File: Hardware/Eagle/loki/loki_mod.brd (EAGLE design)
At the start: 21.9 x 22.9 mm, 39 parts

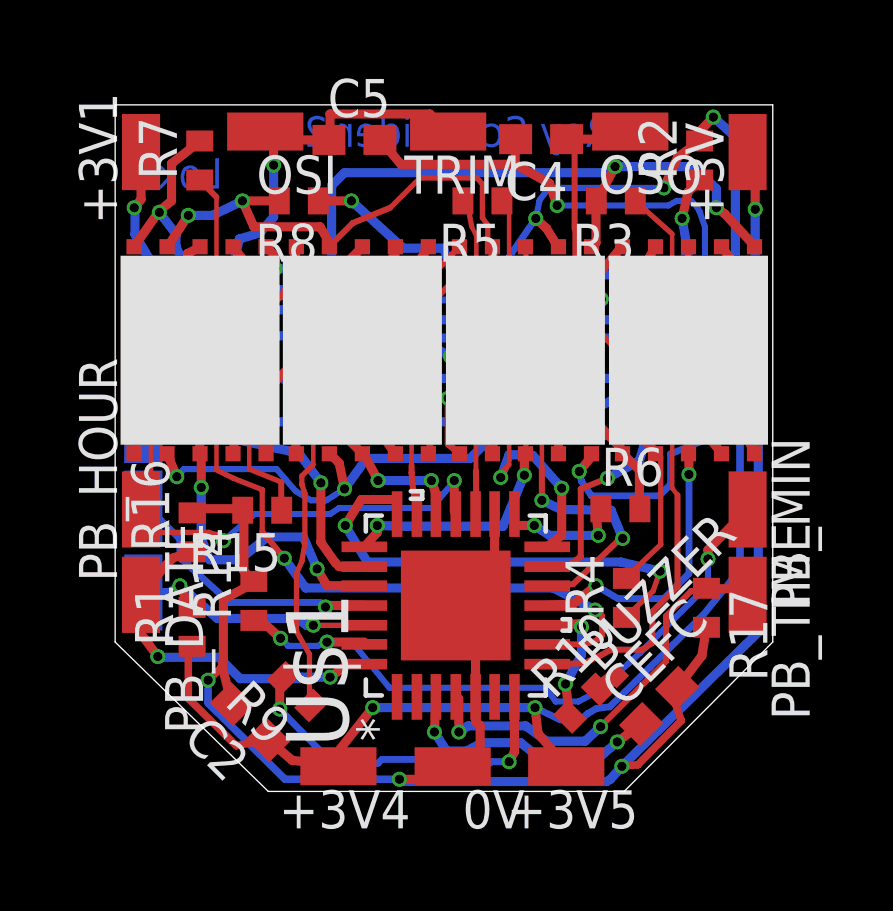
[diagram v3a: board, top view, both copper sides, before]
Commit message: Eliminated one display pin pass-through.
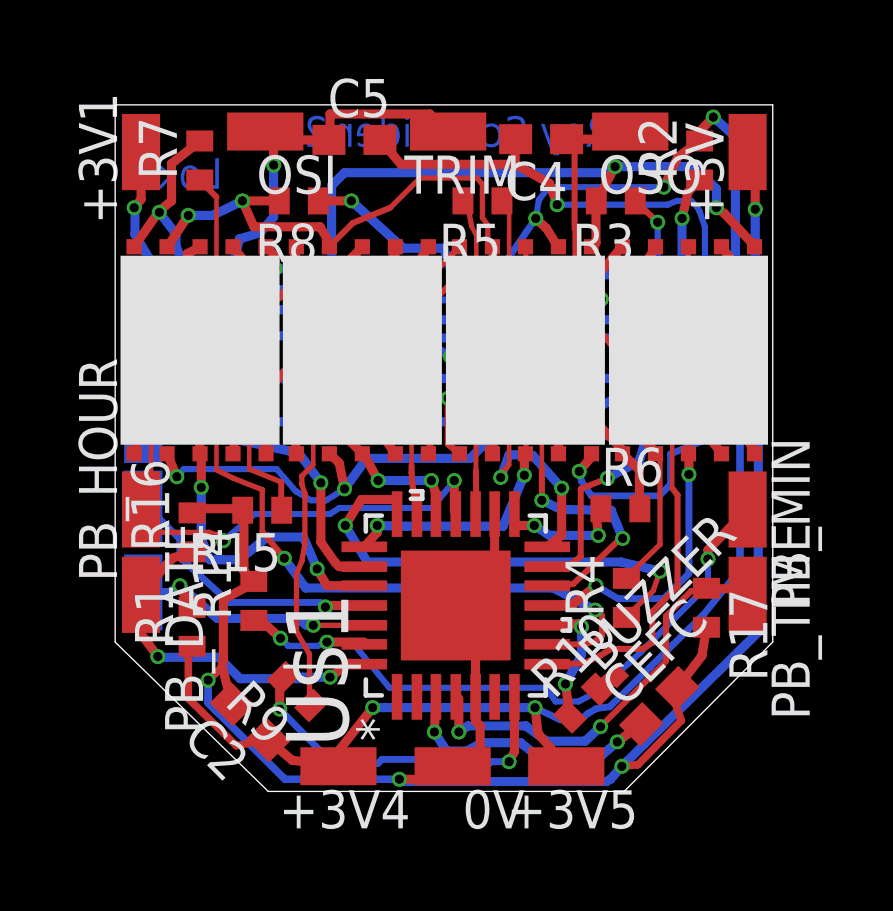
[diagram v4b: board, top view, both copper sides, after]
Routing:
- net RC4/LED_M3: track 20.8 -> 21.5 mm
- net RC5/LED_M2: track 15.2 -> 14.8 mm, vias 2 -> 4
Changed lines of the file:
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@@
 <wire x1="11.176" y1="0.635" x2="11.2268" y2="0.6858" width="0.1524" layer="1"/>
 <wire x1="14.4526" y1="20.1168" x2="13.3096" y2="20.7518" width="0.3048" layer="1"/>
-<wire x1="14.7066" y1="19.3802" x2="14.4526" y2="20.1168" width="0.3048" layer="1"/>
+<wire x1="14.7066" y1="19.4056" x2="14.4526" y2="20.1168" width="0.3048" layer="1"/>
 <wire x1="19.6342" y1="15.6464" x2="19.6342" y2="18.669" width="0.2032" layer="16"/>
 <wire x1="21.4122" y1="14.1986" x2="19.6342" y2="15.6464" width="0.3048" layer="1"/>
@@
 <via x="16.8656" y="0.6858" extent="1-16" drill="0.3048"/>
 <via x="9.4488" y="0.254" extent="1-16" drill="0.3048"/>
-<via x="14.7066" y="19.3802" extent="1-16" drill="0.3048"/>
+<via x="14.7066" y="19.4056" extent="1-16" drill="0.3048"/>
 <via x="19.6342" y="15.6464" extent="1-16" drill="0.3048"/>
 <via x="21.4122" y="12.6238" extent="1-16" drill="0.3048"/>
@@
 <wire x1="19.3802" y1="19.3294" x2="19.177" y2="19.5326" width="0.2032" layer="16"/>
 <wire x1="19.177" y1="19.5326" x2="18.6944" y2="19.5326" width="0.2032" layer="16"/>
-<wire x1="18.6944" y1="19.5326" x2="18.415" y2="19.3802" width="0.2032" layer="16"/>
-<wire x1="18.415" y1="19.3802" x2="14.7066" y2="19.3802" width="0.2032" layer="16"/>
+<wire x1="18.6944" y1="19.5326" x2="18.3896" y2="19.4056" width="0.2032" layer="16"/>
+<wire x1="18.3896" y1="19.4056" x2="14.7066" y2="19.4056" width="0.2032" layer="16"/>
 <wire x1="11.9888" y1="2.9972" x2="11.9888" y2="2.1844" width="0.3048" layer="1"/>
 <wire x1="11.9888" y1="2.1844" x2="12.1412" y2="2.032" width="0.3048" layer="1"/>
@@
 <wire x1="19.0754" y1="19.8374" x2="19.4564" y2="20.2184" width="0.3048" layer="1"/>
 <wire x1="18.8722" y1="18.9484" x2="19.0754" y2="19.8374" width="0.3048" layer="1"/>
-<wire x1="19.0754" y1="17.78" x2="18.8722" y2="18.9484" width="0.3048" layer="16"/>
-<wire x1="17.2974" y1="15.5702" x2="19.0754" y2="17.78" width="0.3048" layer="16"/>
-<wire x1="14.9606" y1="15.5702" x2="17.2974" y2="15.5702" width="0.3048" layer="16"/>
+<wire x1="18.8722" y1="16.891" x2="18.8722" y2="18.9484" width="0.3048" layer="16"/>
+<wire x1="18.6182" y1="15.5702" x2="18.8722" y2="16.891" width="0.3048" layer="16"/>
+<wire x1="14.9606" y1="15.5702" x2="18.6182" y2="15.5702" width="0.3048" layer="16"/>
 <wire x1="14.0716" y1="14.732" x2="14.9606" y2="15.5702" width="0.1778" layer="1"/>
 <wire x1="14.0716" y1="11.684" x2="14.0716" y2="14.732" width="0.1778" layer="1"/>
@@
 <contactref element="U$1" pad="13"/>
 <contactref element="R3" pad="1"/>
-<wire x1="17.907" y1="14.5796" x2="18.542" y2="15.4432" width="0.2032" layer="1"/>
-<wire x1="17.907" y1="12.4206" x2="17.907" y2="14.5796" width="0.2032" layer="1"/>
+<wire x1="17.907" y1="12.4206" x2="17.907" y2="16.256" width="0.2032" layer="1"/>
 <wire x1="17.4498" y1="10.8712" x2="17.907" y2="12.4206" width="0.3048" layer="16"/>
 <wire x1="16.383" y1="10.287" x2="17.4498" y2="10.8712" width="0.3048" layer="16"/>
@@
 <via x="17.907" y="12.4206" extent="1-16" drill="0.3048"/>
 <via x="16.383" y="10.287" extent="1-16" drill="0.3048"/>
-<wire x1="18.542" y1="15.4432" x2="18.542" y2="18.43" width="0.1524" layer="1"/>
-<wire x1="18.542" y1="18.43" x2="17.3124" y2="19.5326" width="0.1778" layer="1"/>
+<via x="17.907" y="16.256" extent="1-16" drill="0.3048"/>
+<wire x1="17.907" y1="16.256" x2="18.1356" y2="17.018" width="0.2032" layer="16"/>
+<wire x1="18.1356" y1="17.018" x2="18.0594" y2="17.7038" width="0.2032" layer="16"/>
+<wire x1="18.0594" y1="17.7038" x2="18.0594" y2="18.8214" width="0.2032" layer="16"/>
+<via x="18.0594" y="18.8214" extent="1-16" drill="0.3048"/>
+<wire x1="18.0594" y1="18.8214" x2="17.3228" y2="19.5222" width="0.2032" layer="1"/>
+<wire x1="17.3228" y1="19.5222" x2="17.3124" y2="19.5326" width="0.1778" layer="1"/>
 </signal>
 <signal name="RC6/LED_M1">
@@
 <wire x1="18.7198" y1="6.6802" x2="17.8816" y2="5.842" width="0.2032" layer="1"/>
 <wire x1="16.8402" y1="14.3256" x2="18.5166" y2="14.3256" width="0.3048" layer="16"/>
-<wire x1="15.2908" y1="16.2306" x2="16.8402" y2="14.3256" width="0.1778" layer="1"/>
+<wire x1="15.2908" y1="16.2306" x2="16.8402" y2="14.3256" width="0.2032" layer="1"/>
 <wire x1="15.2908" y1="21.5392" x2="15.0232" y2="21.59" width="0.1524" layer="1"/>
 <via x="18.5166" y="14.3256" extent="1-16" drill="0.3048"/>
 <via x="16.8402" y="14.3256" extent="1-16" drill="0.3048"/>
 <wire x1="17.8816" y1="5.842" x2="17.8816" y2="4.8006" width="0.2032" layer="1"/>
-<wire x1="17.8816" y1="4.8006" x2="17.5514" y2="4.572" width="0.2032" layer="1"/>
+<wire x1="17.8816" y1="4.8006" x2="17.5514" y2="4.5974" width="0.2032" layer="1"/>
 <wire x1="14.3764" y1="4.0894" x2="15.5956" y2="4.1148" width="0.2032" layer="1"/>
-<wire x1="18.542" y1="9.9568" x2="18.7198" y2="9.7282" width="0.1524" layer="1"/>
+<wire x1="18.542" y1="9.9568" x2="18.7198" y2="9.7282" width="0.2032" layer="1"/>
 <wire x1="18.7198" y1="9.7282" x2="18.7198" y2="6.6802" width="0.2032" layer="1"/>
-<wire x1="18.542" y1="9.9568" x2="18.542" y2="12.4968" width="0.1524" layer="1"/>
-<wire x1="18.542" y1="12.4968" x2="18.4912" y2="12.7" width="0.1524" layer="1"/>
-<wire x1="18.4912" y1="12.7" x2="18.4912" y2="13.7414" width="0.2032" layer="1"/>
-<wire x1="18.4912" y1="13.7414" x2="18.5166" y2="13.7922" width="0.1524" layer="1"/>
-<wire x1="18.5166" y1="13.7922" x2="18.5166" y2="14.3256" width="0.2032" layer="1"/>
+<wire x1="18.542" y1="9.9568" x2="18.542" y2="11.8872" width="0.1524" layer="1"/>
+<wire x1="18.542" y1="11.8872" x2="18.5166" y2="12.0142" width="0.1524" layer="1"/>
 <wire x1="15.2908" y1="21.5392" x2="15.2908" y2="18.5928" width="0.2032" layer="1"/>
 <wire x1="15.2908" y1="18.5928" x2="15.2908" y2="17.3482" width="0.1524" layer="1"/>
 <wire x1="15.2908" y1="17.3482" x2="15.2908" y2="16.2306" width="0.2032" layer="1"/>
 <wire x1="15.5956" y1="4.1148" x2="16.129" y2="4.3688" width="0.2032" layer="1"/>
-<wire x1="16.129" y1="4.3688" x2="16.51" y2="4.572" width="0.2032" layer="1"/>
-<wire x1="16.51" y1="4.572" x2="17.5514" y2="4.572" width="0.2032" layer="1"/>
+<wire x1="16.129" y1="4.3688" x2="16.51" y2="4.5974" width="0.2032" layer="1"/>
+<wire x1="16.51" y1="4.5974" x2="17.5514" y2="4.5974" width="0.2032" layer="1"/>
+<wire x1="18.5166" y1="14.3256" x2="18.5166" y2="12.0142" width="0.2032" layer="1"/>
 </signal>
 <signal name="T1OSI">
@@
 <wire x1="3.3528" y1="10.5664" x2="3.9116" y2="10.287" width="0.1778" layer="1"/>
 <wire x1="3.3528" y1="13.081" x2="3.3528" y2="10.5664" width="0.1524" layer="1"/>
-<wire x1="3.7846" y1="13.8684" x2="3.3528" y2="13.081" width="0.1778" layer="1"/>
+<wire x1="3.7846" y1="13.8684" x2="3.3528" y2="13.081" width="0.2032" layer="1"/>
 <wire x1="3.7846" y1="16.8148" x2="3.7846" y2="13.8684" width="0.2032" layer="1"/>
 <wire x1="4.1148" y1="18.2626" x2="3.7846" y2="16.8148" width="0.3048" layer="16"/>
@@
 <wire x1="11.684" y1="16.2306" x2="12.192" y2="17.3736" width="0.2286" layer="16"/>
 <wire x1="14.732" y1="18.0086" x2="14.7506" y2="18.0046" width="0.1524" layer="1"/>
-<wire x1="14.4272" y1="19.9644" x2="18.2626" y2="19.9644" width="0.2032" layer="16"/>
-<wire x1="14.1224" y1="19.558" x2="14.4272" y2="19.9644" width="0.2032" layer="16"/>
-<wire x1="13.9954" y1="18.9484" x2="14.1224" y2="19.558" width="0.2032" layer="16"/>
+<wire x1="14.4272" y1="19.9898" x2="18.2626" y2="19.9898" width="0.2032" layer="16"/>
+<wire x1="14.097" y1="19.558" x2="14.4272" y2="19.9898" width="0.2032" layer="16"/>
+<wire x1="13.9954" y1="18.9484" x2="14.097" y2="19.558" width="0.2032" layer="16"/>
 <via x="20.6502" y="16.7894" extent="1-16" drill="0.3048"/>
 <via x="19.9136" y="22.3266" extent="1-16" drill="0.3048"/>
@@
 <via x="8.4074" y="16.6116" extent="1-16" drill="0.3048"/>
 <via x="13.9954" y="18.9484" extent="1-16" drill="0.3048"/>
-<via x="18.2626" y="19.9644" extent="1-16" drill="0.3048"/>
-<wire x1="18.2626" y1="19.9644" x2="18.6182" y2="20.7518" width="0.3048" layer="1"/>
+<via x="18.2626" y="19.9898" extent="1-16" drill="0.3048"/>
+<wire x1="18.2626" y1="19.9898" x2="18.6182" y2="20.7518" width="0.3048" layer="1"/>
 <wire x1="18.6182" y1="20.7518" x2="18.7198" y2="20.9804" width="0.3048" layer="1"/>
 <wire x1="18.7198" y1="20.9804" x2="19.4564" y2="21.5288" width="0.3048" layer="1"/>
@@
 <contactref element="1M" pad="2D"/>
 <contactref element="R4" pad="2"/>
-<wire x1="18.161" y1="11.0236" x2="18.0086" y2="11.1252" width="0.1524" layer="1"/>
-<wire x1="18.161" y1="8.0772" x2="18.161" y2="11.0236" width="0.1778" layer="1"/>
-<wire x1="16.9926" y1="6.9596" x2="18.161" y2="8.0772" width="0.1778" layer="1"/>
+<wire x1="18.1356" y1="11.0236" x2="18.0086" y2="11.1252" width="0.1524" layer="1"/>
+<wire x1="18.1356" y1="8.0772" x2="18.1356" y2="11.0236" width="0.1778" layer="1"/>
+<wire x1="16.9926" y1="6.9596" x2="18.1356" y2="8.0772" width="0.1778" layer="1"/>
 <wire x1="18.0086" y1="11.1252" x2="17.9862" y2="11.1046" width="0.1524" layer="1"/>
 <wire x1="16.9926" y1="6.9596" x2="17.018" y2="6.9492" width="0.1778" layer="1"/>
